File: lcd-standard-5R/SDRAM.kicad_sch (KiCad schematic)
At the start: 8 parts, among them U11 MT48LC16M16A2P

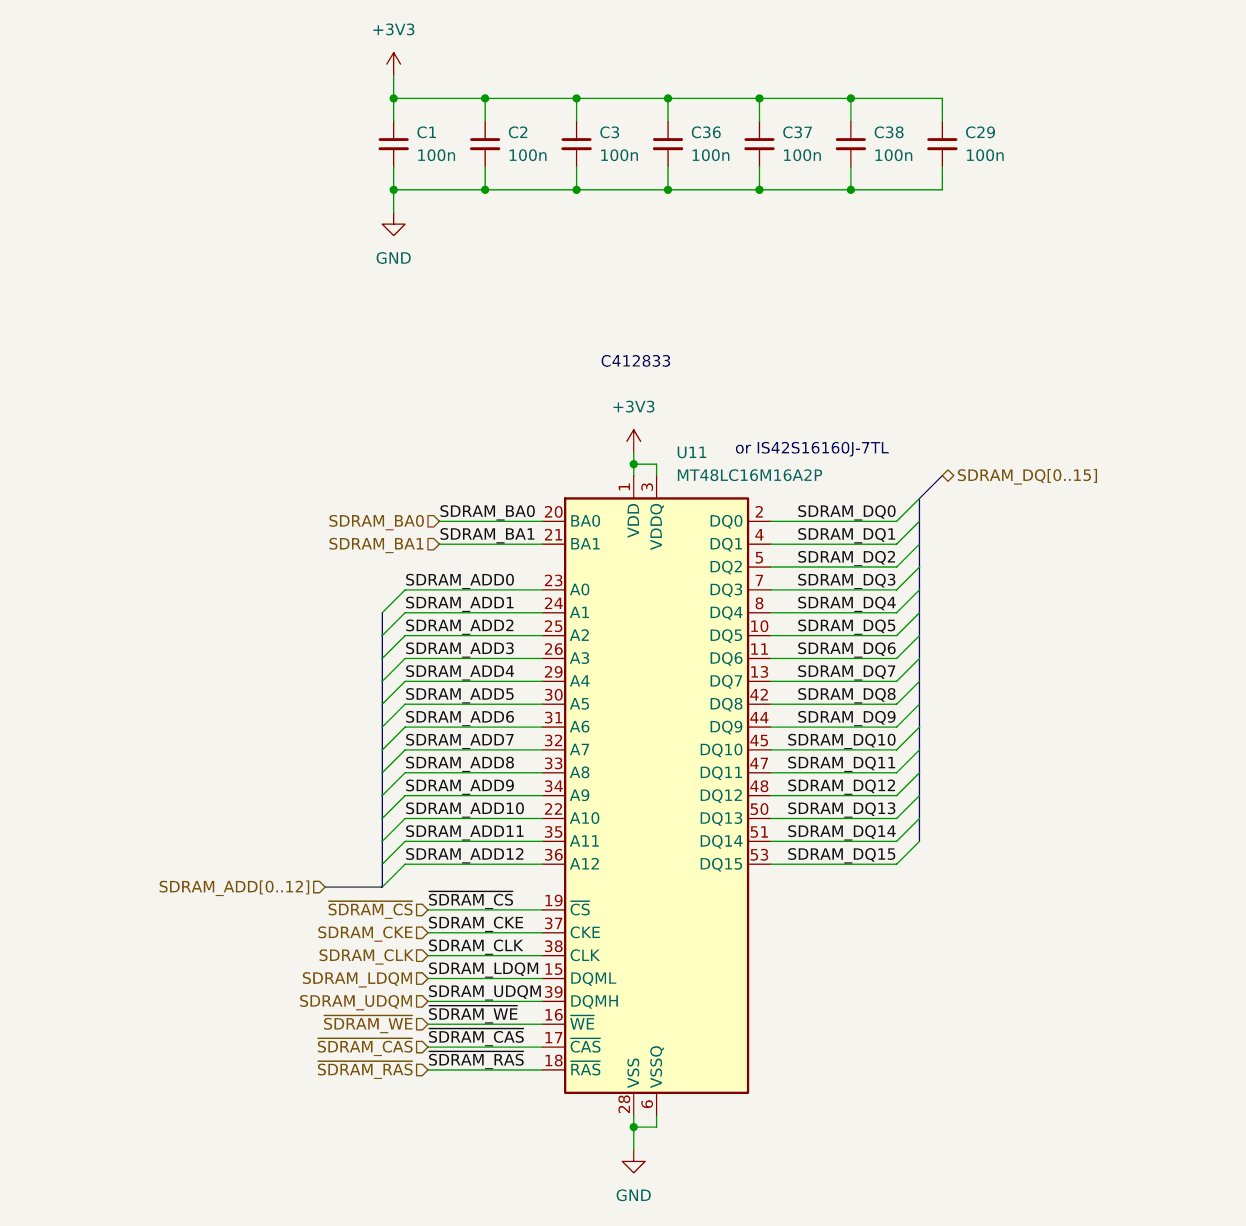
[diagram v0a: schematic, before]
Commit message: Change MCU to STM32H743
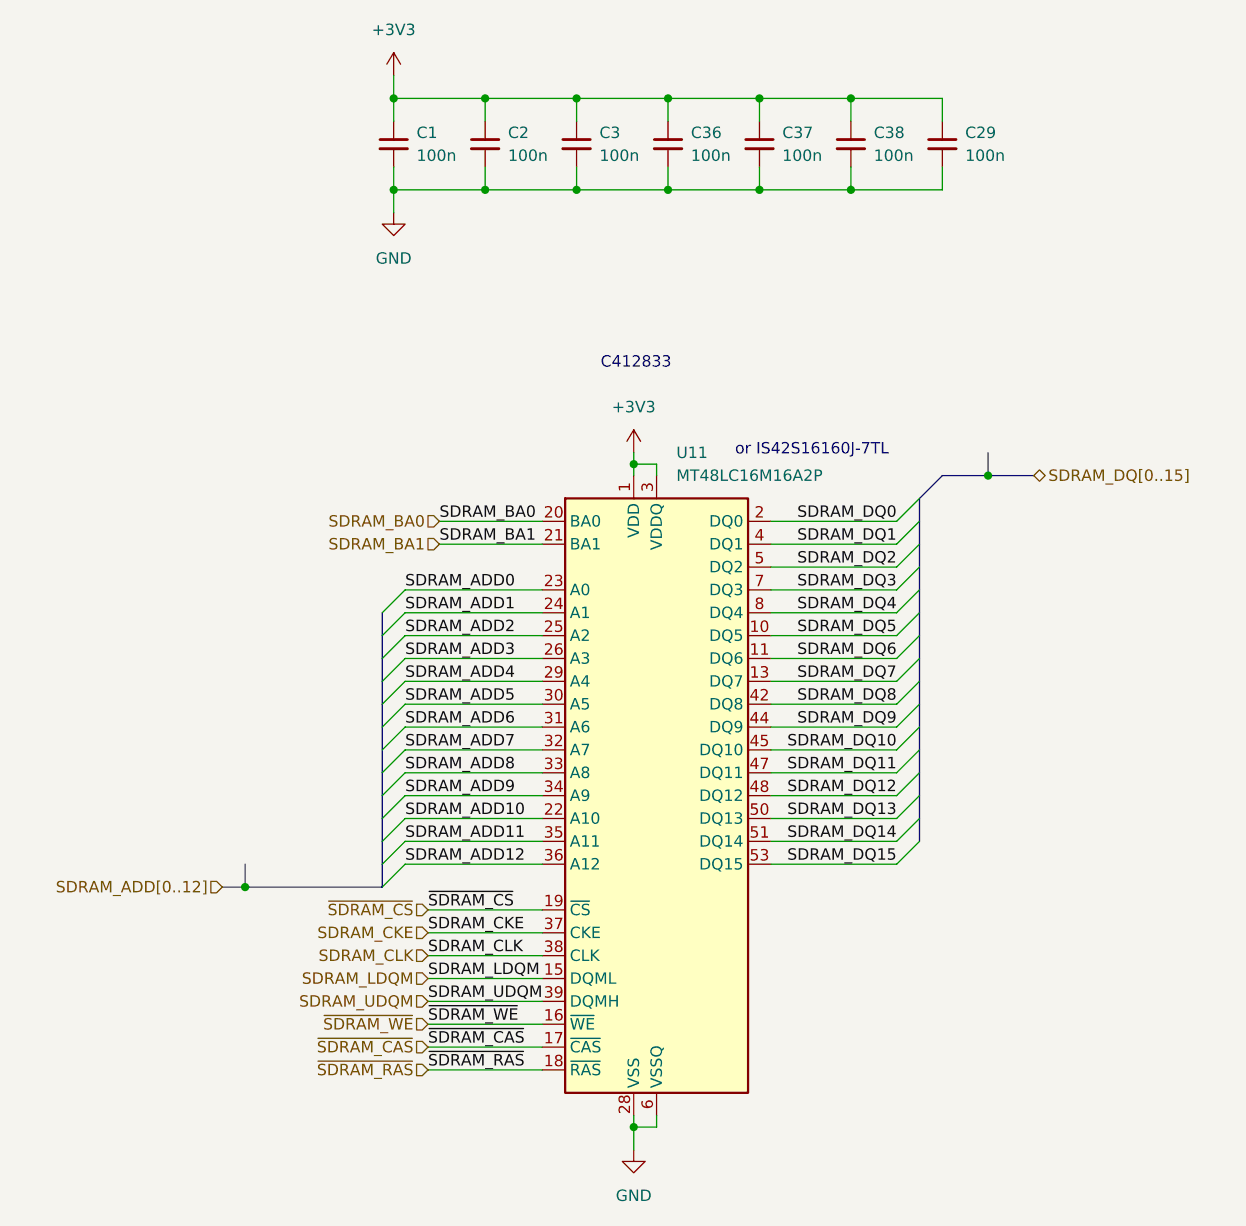
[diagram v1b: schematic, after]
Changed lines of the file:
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@@
+	)
+	(junction
+		(at 181.61 80.01)
+		(diameter 0)
+		(color 0 0 0 0)
+	)
+	(junction
+		(at 99.06 125.73)
+		(diameter 0)
+		(color 0 0 0 0)
 	)
 	(junction
@@
 		)
 	)
+	(bus
+		(pts
+			(xy 176.53 80.01) (xy 181.61 80.01)
+		)
+		(stroke
+			(width 0)
+			(type default)
+		)
+	)
 	(wire
 		(pts
@@
 	(bus
 		(pts
+			(xy 181.61 80.01) (xy 186.69 80.01)
+		)
+		(stroke
+			(width 0)
+			(type default)
+		)
+	)
+	(bus
+		(pts
 			(xy 173.99 110.49) (xy 173.99 107.95)
 		)
@@
 		)
 	)
+	(bus
+		(pts
+			(xy 181.61 77.47) (xy 181.61 80.01)
+		)
+		(stroke
+			(width 0)
+			(type default)
+		)
+	)
 	(wire
 		(pts
@@
 		)
 	)
+	(bus
+		(pts
+			(xy 99.06 123.19) (xy 99.06 125.73)
+		)
+		(stroke
+			(width 0)
+			(type default)
+		)
+	)
 	(wire
 		(pts
@@
 	(bus
 		(pts
+			(xy 99.06 125.73) (xy 114.3 125.73)
+		)
+		(stroke
+			(width 0)
+			(type default)
+		)
+	)
+	(bus
+		(pts
 			(xy 173.99 118.11) (xy 173.99 115.57)
 		)
@@
 	(bus
 		(pts
-			(xy 107.95 125.73) (xy 114.3 125.73)
+			(xy 96.52 125.73) (xy 99.06 125.73)
 		)
 		(stroke
@@
 	(hierarchical_label "SDRAM_ADD[0..12]"
 		(shape input)
-		(at 107.95 125.73 180)
+		(at 96.52 125.73 180)
 		(fields_autoplaced yes)
 		(effects
@@
 	(hierarchical_label "SDRAM_DQ[0..15]"
 		(shape bidirectional)
-		(at 176.53 80.01 0)
+		(at 186.69 80.01 0)
 		(fields_autoplaced yes)
 		(effects
@@
 		)
 	)
+	(netclass_flag ""
+		(length 2.54)
+		(shape round)
+		(at 99.06 123.19 0)
+		(fields_autoplaced yes)
+		(effects
+			(font
+				(size 1.27 1.27)
+			)
+			(justify left bottom)
+		)
+		(property "Netclass" "SDRAM_ADDRESS"
+			(at 98.3615 120.65 0)
+			(effects
+				(font
+					(size 1.27 1.27)
+					(italic yes)
+				)
+				(justify right)
+			)
+		)
+	)
+	(netclass_flag ""
+		(length 2.54)
+		(shape round)
+		(at 181.61 77.47 0)
+		(fields_autoplaced yes)
+		(effects
+			(font
+				(size 1.27 1.27)
+			)
+			(justify left bottom)
+		)
+		(property "Netclass" "SDRAM_DATA"
+			(at 182.3085 74.93 0)
+			(effects
+				(font
+					(size 1.27 1.27)
+					(italic yes)
+				)
+				(justify left)
+			)
+		)
+	)

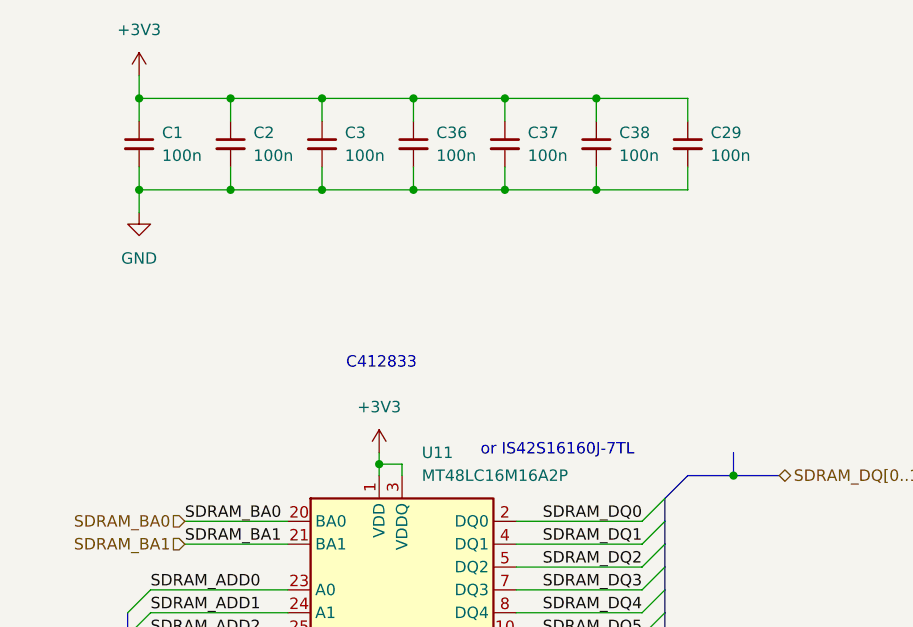
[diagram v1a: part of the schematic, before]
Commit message: Add QSPI Flash trace length matching to 5 inch LCD
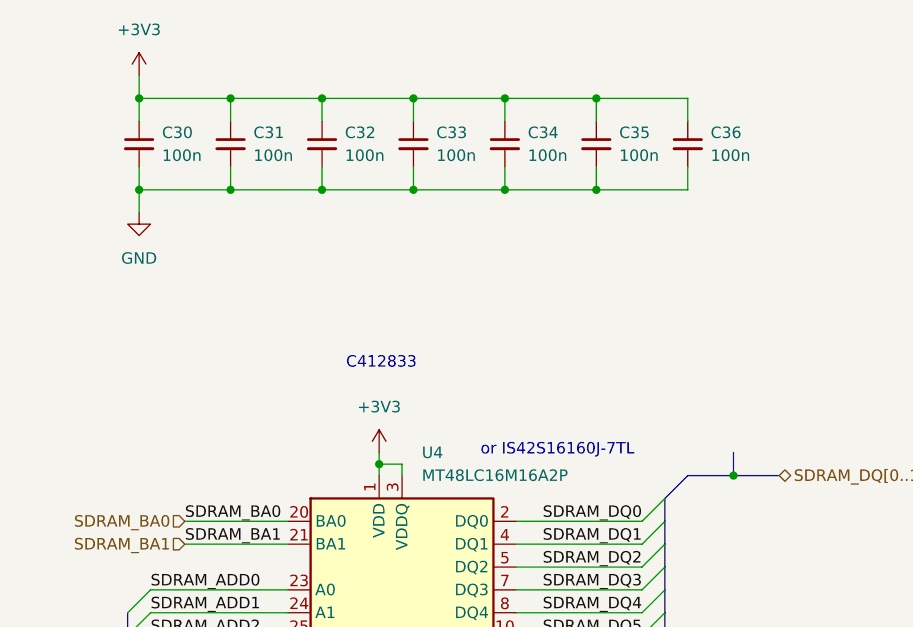
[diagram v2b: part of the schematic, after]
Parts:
- renumbered C1 to C30, C2 to C31, C3 to C32, C36 to C33, C37 to C34, C38 to C35, C29 to C36, U11 to U4
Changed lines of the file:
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@@
 (kicad_sch
-	(version 20231120)
+	(version 20250114)
 	(generator "eeschema")
-	(generator_version "8.0")
+	(generator_version "9.0")
 	(paper "A4")
+	(text "C412833"
+		(exclude_from_sim no)
+		(at 142.494 67.564 0)
+		(effects
+			(font
+				(size 1.27 1.27)
+			)
+		)
+	)
+	(text "or IS42S16160J-7TL"
+		(exclude_from_sim no)
+		(at 162.052 77.216 0)
+		(effects
+			(font
+				(size 1.27 1.27)
+			)
+		)
+	)
 	(junction
 		(at 166.37 48.26)
@@
 		)
 	)
-	(text "C412833"
-		(exclude_from_sim no)
-		(at 142.494 67.564 0)
-		(effects
-			(font
-				(size 1.27 1.27)
-			)
-		)
-	)
-	(text "or IS42S16160J-7TL"
-		(exclude_from_sim no)
-		(at 162.052 77.216 0)
-		(effects
-			(font
-				(size 1.27 1.27)
-			)
-		)
-	)
 	(label "SDRAM_DQ7"
 		(at 171.45 102.87 180)
-		(fields_autoplaced yes)
 		(effects
 			(font
@@
 	(label "SDRAM_ADD4"
 		(at 116.84 102.87 0)
-		(fields_autoplaced yes)
 		(effects
 			(font
@@
 	(label "SDRAM_DQ0"
 		(at 171.45 85.09 180)
-		(fields_autoplaced yes)
 		(effects
 			(font
@@
 	(label "SDRAM_ADD12"
 		(at 116.84 123.19 0)
-		(fields_autoplaced yes)
 		(effects
 			(font
@@
 	(label "SDRAM_DQ3"
 		(at 171.45 92.71 180)
-		(fields_autoplaced yes)
 		(effects
 			(font
@@
 	(label "SDRAM_DQ9"
 		(at 171.45 107.95 180)
-		(fields_autoplaced yes)
 		(effects
 			(font
@@
 	(label "SDRAM_ADD7"
 		(at 116.84 110.49 0)
-		(fields_autoplaced yes)
 		(effects
 			(font
@@
 	(label "SDRAM_ADD8"
 		(at 116.84 113.03 0)
-		(fields_autoplaced yes)
 		(effects
 			(font
@@
 	(label "SDRAM_ADD11"
 		(at 116.84 120.65 0)
-		(fields_autoplaced yes)
 		(effects
 			(font
@@
 	(label "SDRAM_DQ14"
 		(at 171.45 120.65 180)
-		(fields_autoplaced yes)
 		(effects
 			(font
@@
 	(label "SDRAM_UDQM"
 		(at 119.38 138.43 0)
-		(fields_autoplaced yes)
 		(effects
 			(font
@@
 	(label "SDRAM_ADD10"
 		(at 116.84 118.11 0)
-		(fields_autoplaced yes)
 		(effects
 			(font
@@
 	(label "SDRAM_DQ11"
 		(at 171.45 113.03 180)
-		(fields_autoplaced yes)
 		(effects
 			(font
@@
 	(label "SDRAM_ADD1"
 		(at 116.84 95.25 0)
-		(fields_autoplaced yes)
 		(effects
 			(font
@@
 	(label "SDRAM_DQ1"
 		(at 171.45 87.63 180)
-		(fields_autoplaced yes)
 		(effects
 			(font
@@
 	(label "SDRAM_BA1"
 		(at 120.65 87.63 0)
-		(fields_autoplaced yes)
 		(effects
 			(font
@@
 	(label "SDRAM_DQ8"
 		(at 171.45 105.41 180)
-		(fields_autoplaced yes)
 		(effects
 			(font
@@
 	(label "SDRAM_DQ12"
 		(at 171.45 115.57 180)
-		(fields_autoplaced yes)
 		(effects
 			(font
@@
 	(label "SDRAM_DQ15"
 		(at 171.45 123.19 180)
-		(fields_autoplaced yes)
 		(effects
 			(font
@@
 	(label "SDRAM_DQ4"
 		(at 171.45 95.25 180)
-		(fields_autoplaced yes)
 		(effects
 			(font
@@
 	(label "~{SDRAM_CS}"
 		(at 119.38 128.27 0)
-		(fields_autoplaced yes)
 		(effects
 			(font
@@
 	(label "SDRAM_ADD6"
 		(at 116.84 107.95 0)
-		(fields_autoplaced yes)
 		(effects
 			(font
@@
 	(label "SDRAM_ADD5"
 		(at 116.84 105.41 0)
-		(fields_autoplaced yes)
 		(effects
 			(font
@@
 	(label "SDRAM_ADD2"
 		(at 116.84 97.79 0)
-		(fields_autoplaced yes)
 		(effects
 			(font
@@
 	(label "SDRAM_DQ2"
 		(at 171.45 90.17 180)
-		(fields_autoplaced yes)
 		(effects
 			(font
@@
 	(label "~{SDRAM_RAS}"
 		(at 119.38 146.05 0)
-		(fields_autoplaced yes)
 		(effects
 			(font
@@
 	(label "~{SDRAM_CAS}"
 		(at 119.38 143.51 0)
-		(fields_autoplaced yes)
 		(effects
 			(font
@@
 	(label "SDRAM_LDQM"
 		(at 119.38 135.89 0)
-		(fields_autoplaced yes)
 		(effects
 			(font
@@
 	(label "SDRAM_ADD3"
 		(at 116.84 100.33 0)
-		(fields_autoplaced yes)
 		(effects
 			(font
@@
 	(label "SDRAM_CLK"
 		(at 119.38 133.35 0)
-		(fields_autoplaced yes)
 		(effects
 			(font
@@
 	(label "SDRAM_DQ13"
 		(at 171.45 118.11 180)
-		(fields_autoplaced yes)
 		(effects
 			(font
@@
 	(label "SDRAM_CKE"
 		(at 119.38 130.81 0)
-		(fields_autoplaced yes)
 		(effects
 			(font
@@
 	(label "~{SDRAM_WE}"
 		(at 119.38 140.97 0)
-		(fields_autoplaced yes)
 		(effects
 			(font
@@
 	(label "SDRAM_DQ5"
 		(at 171.45 97.79 180)
-		(fields_autoplaced yes)
 		(effects
 			(font
@@
 	(label "SDRAM_BA0"
 		(at 120.65 85.09 0)
-		(fields_autoplaced yes)
 		(effects
 			(font
@@
 	(label "SDRAM_ADD9"
 		(at 116.84 115.57 0)
-		(fields_autoplaced yes)
 		(effects
 			(font
@@
 	(label "SDRAM_DQ10"
 		(at 171.45 110.49 180)
-		(fields_autoplaced yes)
 		(effects
 			(font
@@
 	(label "SDRAM_DQ6"
 		(at 171.45 100.33 180)
-		(fields_autoplaced yes)
 		(effects
 			(font
@@
 	(label "SDRAM_ADD0"
 		(at 116.84 92.71 0)
-		(fields_autoplaced yes)
 		(effects
 			(font
@@
 		(shape input)
 		(at 119.38 130.81 180)
-		(fields_autoplaced yes)
 		(effects
 			(font
@@
 		(shape input)
 		(at 119.38 140.97 180)
-		(fields_autoplaced yes)
 		(effects
 			(font
@@
 		(shape input)
 		(at 96.52 125.73 180)
-		(fields_autoplaced yes)
 		(effects
 			(font
@@
 		(shape bidirectional)
 		(at 186.69 80.01 0)
-		(fields_autoplaced yes)
 		(effects
 			(font
@@
 		(shape input)
 		(at 119.38 138.43 180)
-		(fields_autoplaced yes)
 		(effects
 			(font
@@
 		(shape input)
 		(at 119.38 133.35 180)
-		(fields_autoplaced yes)
 		(effects
 			(font
@@
 		(shape input)
 		(at 119.38 143.51 180)
-		(fields_autoplaced yes)
 		(effects
 			(font
@@
 		(shape input)
 		(at 119.38 146.05 180)
-		(fields_autoplaced yes)
 		(effects
 			(font
@@
 		(shape input)
 		(at 119.38 128.27 180)
-		(fields_autoplaced yes)
 		(effects
 			(font
@@
 		(shape input)
 		(at 120.65 85.09 180)
-		(fields_autoplaced yes)
 		(effects
 			(font
@@
 		(shape input)
 		(at 120.65 87.63 180)
-		(fields_autoplaced yes)
 		(effects
 			(font
@@
 		(shape input)
 		(at 119.38 135.89 180)
-		(fields_autoplaced yes)
 		(effects
 			(font
@@
 		(dnp no)
 		(fields_autoplaced yes)
-		(property "Reference" "#PWR0121"
+		(property "Reference" "#PWR055"
 			(at 142.24 161.29 0)
 			(effects
@@
 		(dnp no)
 		(fields_autoplaced yes)
-		(property "Reference" "C3"
+		(property "Reference" "C32"
 			(at 138.43 41.9163 0)
 			(effects
@@
 		(dnp no)
 		(fields_autoplaced yes)
-		(property "Reference" "C29"
+		(property "Reference" "C36"
 			(at 179.07 41.9163 0)
 			(effects
@@
 		(dnp no)
 		(fields_autoplaced yes)
-		(property "Reference" "#PWR0120"
+		(property "Reference" "#PWR054"
 			(at 142.24 81.28 0)
 			(effects
@@
 		(dnp no)
 		(fields_autoplaced yes)
-		(property "Reference" "C37"
+		(property "Reference" "C34"
 			(at 158.75 41.9163 0)
 			(effects
@@
 		(dnp no)
 		(fields_autoplaced yes)
-		(property "Reference" "C38"
+		(property "Reference" "C35"
 			(at 168.91 41.9163 0)
 			(effects
@@
 		(dnp no)
 		(fields_autoplaced yes)
-		(property "Reference" "C2"
+		(property "Reference" "C31"
 			(at 128.27 41.9163 0)
 			(effects
@@
 		(dnp no)
 		(fields_autoplaced yes)
-		(property "Reference" "C36"
+		(property "Reference" "C33"
 			(at 148.59 41.9163 0)
 			(effects
@@
 		(dnp no)
 		(fields_autoplaced yes)
-		(property "Reference" "#PWR02"
+		(property "Reference" "#PWR053"
 			(at 115.57 57.15 0)
 			(effects
@@
 		(dnp no)
 		(fields_autoplaced yes)
-		(property "Reference" "#PWR01"
+		(property "Reference" "#PWR052"
 			(at 115.57 39.37 0)
 			(effects
@@
 		(dnp no)
 		(fields_autoplaced yes)
-		(property "Reference" "U11"
+		(property "Reference" "U4"
 			(at 146.9741 77.47 0)
 			(effects
@@
 		(dnp no)
 		(fields_autoplaced yes)
-		(property "Reference" "C1"
+		(property "Reference" "C30"
 			(at 118.11 41.9163 0)
 			(effects
